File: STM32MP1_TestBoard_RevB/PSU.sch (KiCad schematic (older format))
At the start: 22 parts, among them J9 Barrel_Jack, Q1 DMG2302U, U3 SE8233X2, U4 TPS54202DDC

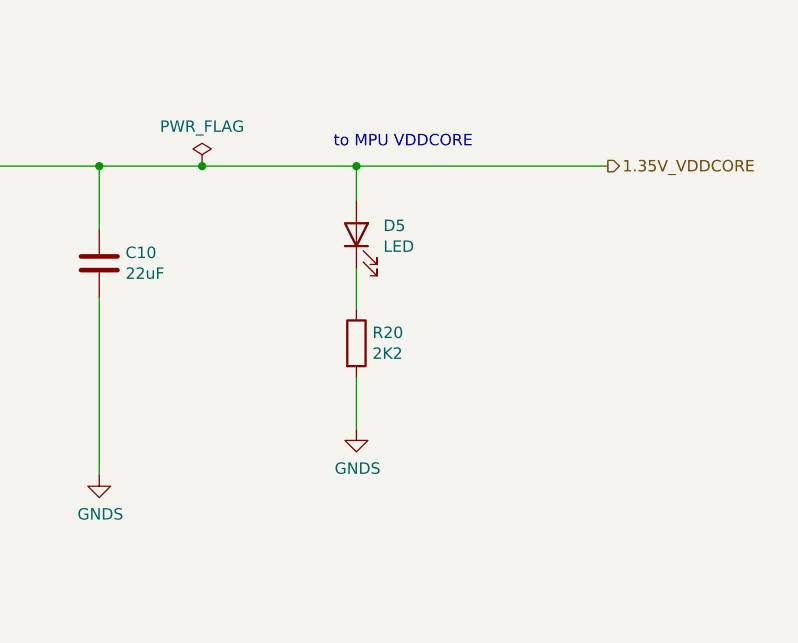
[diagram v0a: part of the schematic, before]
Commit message: Removed 1.35V led and unused DDR capacitors
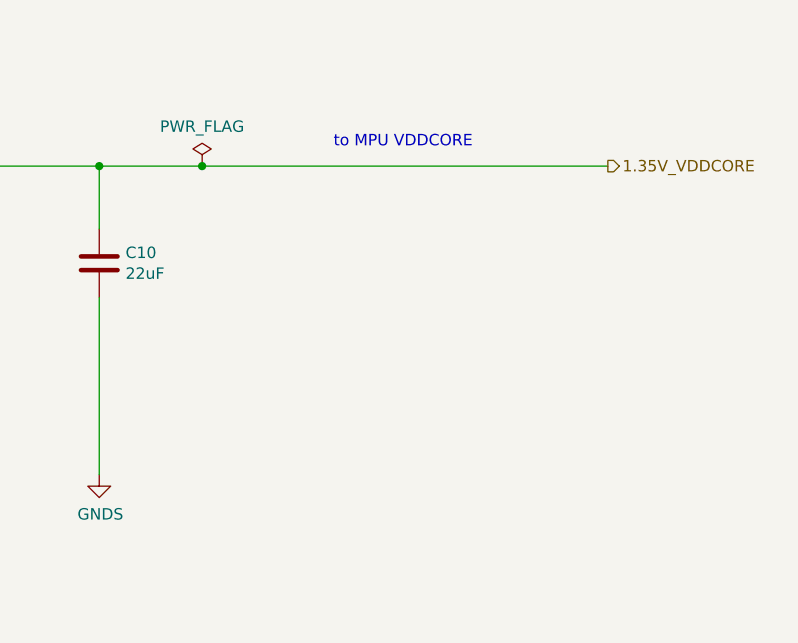
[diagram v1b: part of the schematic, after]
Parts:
- removed D5: LED, LED_SMD:LED_0805_2012Metric_Pad1.15x1.40mm_HandSolder, symbol Device:LED
- removed R20: 2K2, Resistor_SMD:R_0402_1005Metric_Pad0.72x0.64mm_HandSolder, symbol Device:R
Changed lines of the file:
@@
 Connection ~ 10950 4500
-Wire Wire Line
-	10950 4500 11625 4500
 Wire Wire Line
 	6250 8100 7575 8100
@@
 $EndComp
 $Comp
-L Device:LED D5
-U 1 1 5FCE57D0
-P 11625 4800
-F 0 "D5" V 11664 4682 50  0000 R CNN
-F 1 "LED" V 11573 4682 50  0000 R CNN
-F 2 "LED_SMD:LED_0805_2012Metric_Pad1.15x1.40mm_HandSolder" H 11625 4800 50  0001 C CNN
-F 3 "~" H 11625 4800 50  0001 C CNN
-F 4 "~" H 11625 4800 50  0001 C CNN "Mfr"
-F 5 "~" H 11625 4800 50  0001 C CNN "PartNo"
-	1    11625 4800
-	0    -1   -1   0
-$EndComp
-Wire Wire Line
-	11625 4650 11625 4500
-Wire Wire Line
-	11625 4950 11625 5125
-$Comp
-L Device:R R20
-U 1 1 5FCE57DA
-P 11625 5275
-F 0 "R20" H 11695 5321 50  0000 L CNN
-F 1 "2K2" H 11695 5230 50  0000 L CNN
-F 2 "Resistor_SMD:R_0402_1005Metric_Pad0.72x0.64mm_HandSolder" V 11555 5275 50  0001 C CNN
-F 3 "~" H 11625 5275 50  0001 C CNN
-F 4 "~" H 11625 5275 50  0001 C CNN "Mfr"
-F 5 "~" H 11625 5275 50  0001 C CNN "PartNo"
-	1    11625 5275
-	1    0    0    -1
-$EndComp
-Wire Wire Line
-	11625 5425 11625 5650
-$Comp
-L power:GNDS #PWR04
-U 1 1 5FCE57E1
-P 11625 5650
-F 0 "#PWR04" H 11625 5400 50  0001 C CNN
-F 1 "GNDS" H 11630 5477 50  0000 C CNN
-F 2 "" H 11625 5650 50  0001 C CNN
-F 3 "" H 11625 5650 50  0001 C CNN
-	1    11625 5650
-	1    0    0    -1
-$EndComp
-Connection ~ 11625 4500
-Wire Wire Line
-	11625 4500 12725 4500
-$Comp
 L Device:LED D3
 U 1 1 5FCE9C97
@@
 Connection ~ 6250 8100
 NoConn ~ 5750 4600
+Wire Wire Line
+	10950 4500 12725 4500
 $EndSCHEMATC

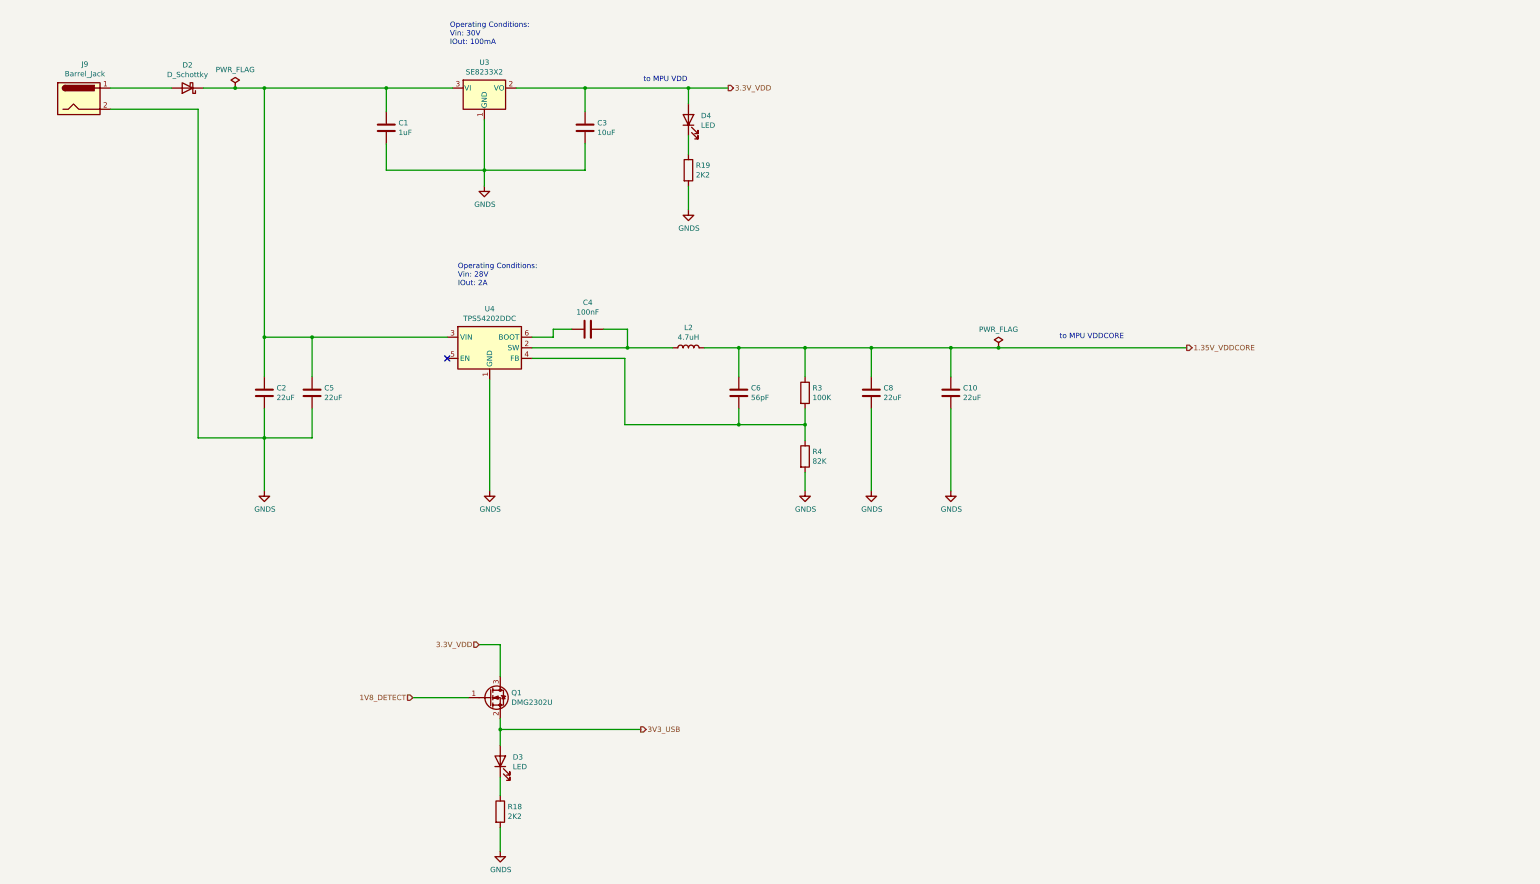
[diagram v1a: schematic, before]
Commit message: Updated design
- Added Crystal/Oscillators
- Replaced both SDMMC with single SDMMC w/ detect pin
- Added USB Type C for VIN
- Moved SWD pins
- Tidied up silk screen for pin headers J1, J2, J3, J4
- Moved DSI socket
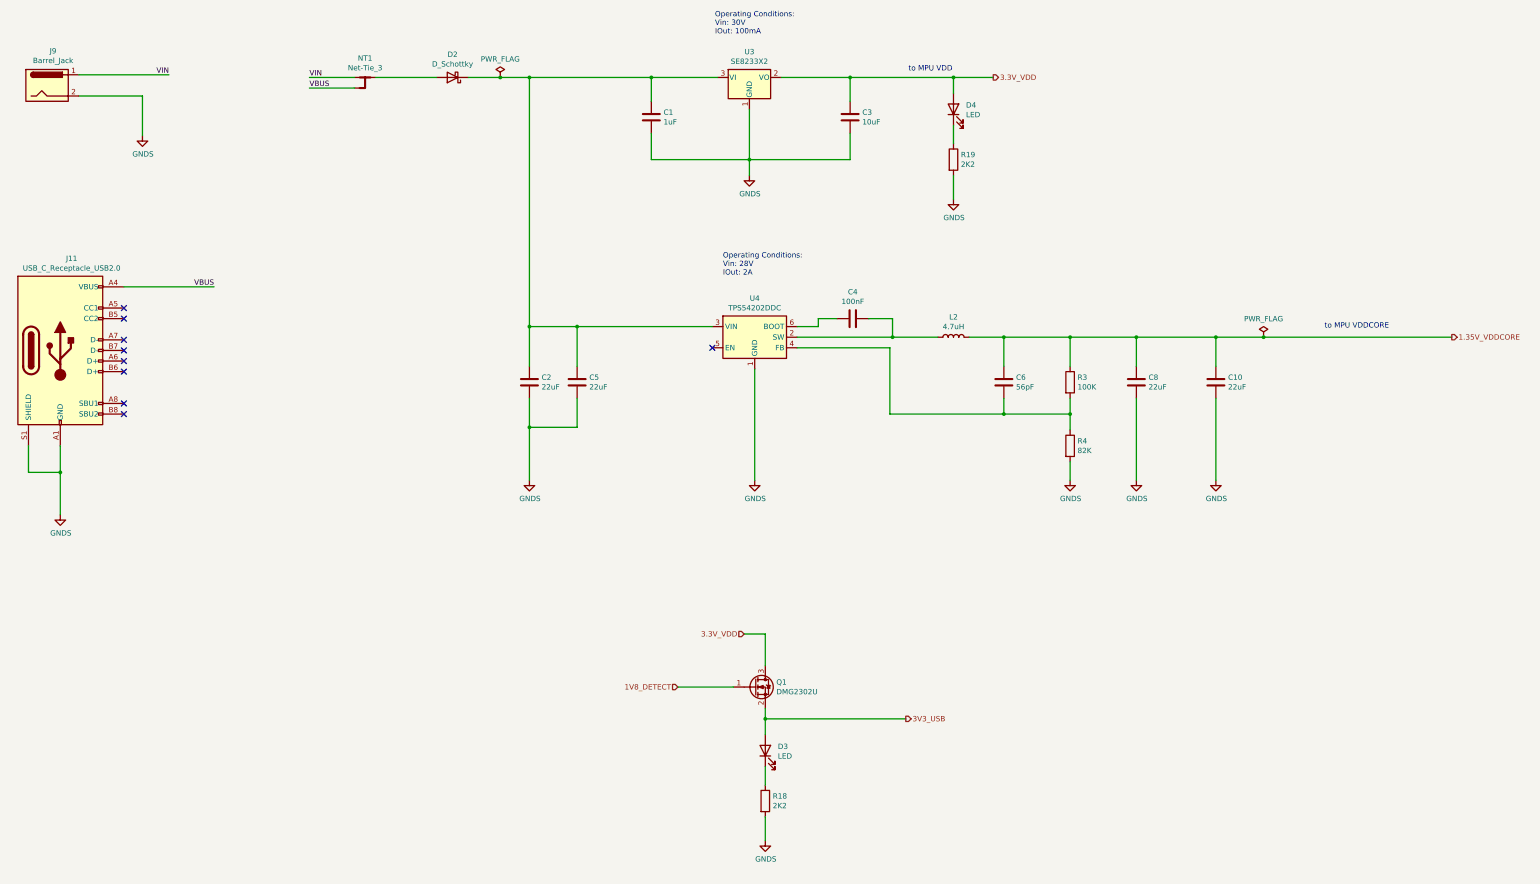
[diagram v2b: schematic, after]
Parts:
- added J11: USB_C_Receptacle_USB2.0, MolexUSB_TypeC:213716-0001_THT_Socket_RightAngle, symbol Connector:USB_C_Receptacle_USB2.0
- added NT1: Net-Tie_3, NetTie:NetTie-3_SMD_Pad0.5mm, symbol Device:Net-Tie_3
- C1: footprint Capacitor_SMD:C_0402_1005Metric_Pad0.74x0.62mm_HandSolder -> Capacitor_SMD:C_0805_2012Metric_Pad1.18x1.45mm_HandSolder; LCSC (none) -> C52923
- C3: footprint Capacitor_SMD:C_0402_1005Metric_Pad0.74x0.62mm_HandSolder -> Capacitor_SMD:C_0805_2012Metric_Pad1.18x1.45mm_HandSolder
- C4: LCSC (none) -> C49678
- C6: LCSC (none) -> C1828
- D3, D4: LCSC (none) -> C84256
- R3: LCSC (none) -> C17407
- R4: LCSC (none) -> C17840
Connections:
- net GNDS: now also J11.A1 (GND), J11.A12 (GND), J11.B1 (GND), J11.B12 (GND), J11.S1 (SHIELD)
- net at D2.2 (A): now also NT1.2; no longer J9.1
- new net VBUS: J11.A4 (VBUS), J11.A9 (VBUS), J11.B4 (VBUS), J11.B9 (VBUS), NT1.3
- new net VIN: J9.1, NT1.1
- no-connect marks 1 -> 9
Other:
- moved on the sheet: C1, C10, C2, C3, C4, C5, C6, C8, D2, D3, D4, J9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

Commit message: completed revb layout
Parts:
- removed D2: D_Schottky, Diode_SMD:D_SOD-123F, symbol Device:D_Schottky
- removed Q1: DMG2302U, Package_TO_SOT_SMD:SOT-23, symbol Device:Q_NMOS_GSD
- added C39, C43: 2.2uF, Capacitor_SMD:C_0805_2012Metric_Pad1.18x1.45mm_HandSolder, symbol Device:C
- added C41, C44: 100nF, Capacitor_SMD:C_0402_1005Metric_Pad0.74x0.62mm_HandSolder, symbol Device:C
- added D2: LED, LED_SMD:LED_0805_2012Metric_Pad1.15x1.40mm_HandSolder, symbol Device:LED
- added R26: 2K2, Resistor_SMD:R_0402_1005Metric_Pad0.72x0.64mm_HandSolder, symbol Device:R
- added U5, U6: SiP3250x, Package_TO_SOT_SMD:SOT-23-6_Handsoldering, symbol SiP3250x:SiP3250x
- C1: LCSC C52923 -> C28323
- J11: Mfr (none) -> Molex; Mouser (none) -> 538-213716-0001; PartNo (none) -> 213716-0001
- R18, R19: LCSC (none) -> C25879
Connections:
- net 1.35V_VDDCORE: now also U6.3 (EN)
- net 1V8_DETECT: now also U5.3 (EN)
- net 3.3V_VDD: now also C39.1, C43.1, U5.5 (IN), U5.6 (IN), U6.5 (IN), U6.6 (IN)
- net 3V3_USB: now also C41.1, U5.1 (OUT), U5.2 (OUT)
- net GNDS: now also C39.2, C41.2, C43.2, C44.2, R26.2, U5.4 (GND), U6.4 (GND)
- net at C1.1, C2.1, C5.1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: now also NT1.2
- new net: C44.1, D2.2 (A), U6.1 (OUT), U6.2 (OUT)
- new net: D2.1 (K), R26.1
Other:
- note added: "1A Required"
- note added: "6.6mA Required Max"
- note removed: "to MPU VDD"
- note removed: "to MPU VDDCORE"
- moved on the sheet: D3, R18

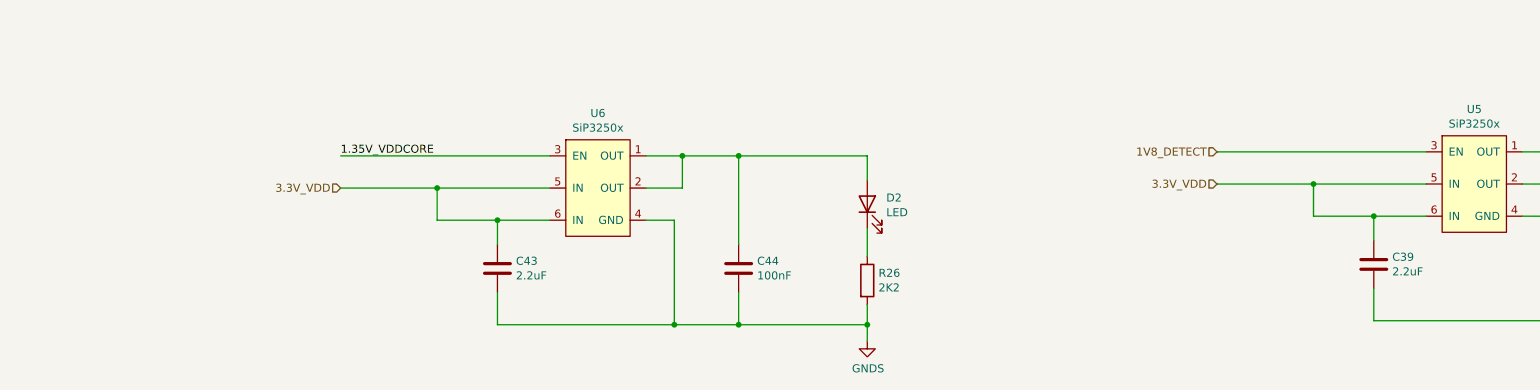
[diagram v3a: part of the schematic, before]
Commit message: updated revb
- Fixed MIPI DSI differential trace spacings. 
- Moved passive components onto back of pcb
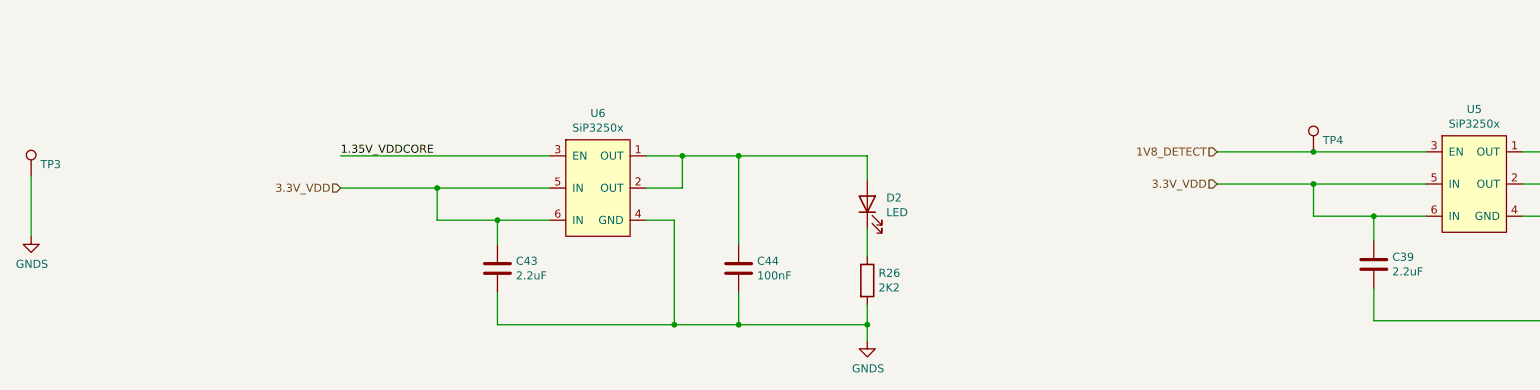
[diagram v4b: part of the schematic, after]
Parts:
- added TP3, TP4: TestPoint, TestPoint:TestPoint_Pad_D1.0mm, symbol Connector:TestPoint
- C1: footprint Capacitor_SMD:C_0805_2012Metric_Pad1.18x1.45mm_HandSolder -> Capacitor_SMD:C_0402_1005Metric_Pad0.74x0.62mm_HandSolder; LCSC C28323 -> C52923
- C3: footprint Capacitor_SMD:C_0805_2012Metric_Pad1.18x1.45mm_HandSolder -> Capacitor_SMD:C_0402_1005Metric_Pad0.74x0.62mm_HandSolder; LCSC (none) -> C15525
- C39, C43: footprint Capacitor_SMD:C_0805_2012Metric_Pad1.18x1.45mm_HandSolder -> Capacitor_SMD:C_0603_1608Metric_Pad1.08x0.95mm_HandSolder; LCSC C49217 -> C23630
- C4: footprint Capacitor_SMD:C_0805_2012Metric_Pad1.18x1.45mm_HandSolder -> Capacitor_SMD:C_0402_1005Metric_Pad0.74x0.62mm_HandSolder; LCSC C49678 -> C1525
- C6: footprint Capacitor_SMD:C_0805_2012Metric_Pad1.18x1.45mm_HandSolder -> Capacitor_SMD:C_0402_1005Metric_Pad0.74x0.62mm_HandSolder; LCSC C1828 -> C1572
- R3: footprint Resistor_SMD:R_0805_2012Metric_Pad1.20x1.40mm_HandSolder -> Resistor_SMD:R_0402_1005Metric_Pad0.72x0.64mm_HandSolder; LCSC C17407 -> C25741
- R4: footprint Resistor_SMD:R_0805_2012Metric_Pad1.20x1.40mm_HandSolder -> Resistor_SMD:R_0402_1005Metric_Pad0.72x0.64mm_HandSolder; LCSC C17840 -> C1542
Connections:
- net 1V8_DETECT: now also TP4.1
- net GNDS: now also TP3.1
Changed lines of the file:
@@
 F 0 "C4" V 9323 4225 50  0000 C CNN
 F 1 "100nF" V 9414 4225 50  0000 C CNN
-F 2 "Capacitor_SMD:C_0805_2012Metric_Pad1.18x1.45mm_HandSolder" H 9613 4075 50  0001 C CNN
+F 2 "Capacitor_SMD:C_0402_1005Metric_Pad0.74x0.62mm_HandSolder" H 9613 4075 50  0001 C CNN
 F 3 "~" H 9575 4225 50  0001 C CNN
 F 4 "~" H 9575 4225 50  0001 C CNN "Mfr"
 F 5 "~" H 9575 4225 50  0001 C CNN "PartNo"
-F 6 "C49678" H 9575 4225 50  0001 C CNN "LCSC"
+F 6 "C1525" H 9575 4225 50  0001 C CNN "LCSC"
 F 7 "~" H 9575 4225 50  0001 C CNN "Comment"
 F 8 "~" H 9575 4225 50  0001 C CNN "Mouser"
@@
 F 0 "C6" H 10885 4779 50  0000 R CNN
 F 1 "56pF" H 10885 4870 50  0000 R CNN
-F 2 "Capacitor_SMD:C_0805_2012Metric_Pad1.18x1.45mm_HandSolder" H 11038 4675 50  0001 C CNN
+F 2 "Capacitor_SMD:C_0402_1005Metric_Pad0.74x0.62mm_HandSolder" H 11038 4675 50  0001 C CNN
 F 3 "~" H 11000 4825 50  0001 C CNN
 F 4 "~" H 11000 4825 50  0001 C CNN "Mfr"
 F 5 "~" H 11000 4825 50  0001 C CNN "PartNo"
-F 6 "C1828" H 11000 4825 50  0001 C CNN "LCSC"
+F 6 "C1572" H 11000 4825 50  0001 C CNN "LCSC"
 F 7 "~" H 11000 4825 50  0001 C CNN "Comment"
 F 8 "~" H 11000 4825 50  0001 C CNN "Mouser"
@@
 F 0 "R3" H 11695 4871 50  0000 L CNN
 F 1 "100K" H 11695 4780 50  0000 L CNN
-F 2 "Resistor_SMD:R_0805_2012Metric_Pad1.20x1.40mm_HandSolder" V 11555 4825 50  0001 C CNN
+F 2 "Resistor_SMD:R_0402_1005Metric_Pad0.72x0.64mm_HandSolder" V 11555 4825 50  0001 C CNN
 F 3 "~" H 11625 4825 50  0001 C CNN
 F 4 "~" H 11625 4825 50  0001 C CNN "Mfr"
 F 5 "~" H 11625 4825 50  0001 C CNN "PartNo"
-F 6 "C17407" H 11625 4825 50  0001 C CNN "LCSC"
+F 6 "C25741" H 11625 4825 50  0001 C CNN "LCSC"
 F 7 "~" H 11625 4825 50  0001 C CNN "Comment"
 F 8 "~" H 11625 4825 50  0001 C CNN "Mouser"
@@
 F 0 "R4" H 11695 5471 50  0000 L CNN
 F 1 "82K" H 11695 5380 50  0000 L CNN
-F 2 "Resistor_SMD:R_0805_2012Metric_Pad1.20x1.40mm_HandSolder" V 11555 5425 50  0001 C CNN
+F 2 "Resistor_SMD:R_0402_1005Metric_Pad0.72x0.64mm_HandSolder" V 11555 5425 50  0001 C CNN
 F 3 "~" H 11625 5425 50  0001 C CNN
 F 4 "~" H 11625 5425 50  0001 C CNN "Mfr"
 F 5 "~" H 11625 5425 50  0001 C CNN "PartNo"
-F 6 "C17840" H 11625 5425 50  0001 C CNN "LCSC"
+F 6 "C1542" H 11625 5425 50  0001 C CNN "LCSC"
 F 7 "~" H 11625 5425 50  0001 C CNN "Comment"
 F 8 "~" H 11625 5425 50  0001 C CNN "Mouser"
@@
 Text HLabel 12900 7675 2    50   Output ~ 0
 3V3_USB
-Wire Wire Line
-	10400 7675 9100 7675
 $Comp
 L power:PWR_FLAG #FLG0102
@@
 F 0 "C1" H 7790 2371 50  0000 L CNN
 F 1 "1uF" H 7790 2280 50  0000 L CNN
-F 2 "Capacitor_SMD:C_0805_2012Metric_Pad1.18x1.45mm_HandSolder" H 7713 2175 50  0001 C CNN
+F 2 "Capacitor_SMD:C_0402_1005Metric_Pad0.74x0.62mm_HandSolder" H 7713 2175 50  0001 C CNN
 F 3 "~" H 7675 2325 50  0001 C CNN
 F 4 "~" H 7675 2325 50  0001 C CNN "Mfr"
 F 5 "~" H 7675 2325 50  0001 C CNN "PartNo"
-F 6 "C28323" H 7675 2325 50  0001 C CNN "LCSC"
+F 6 "C52923" H 7675 2325 50  0001 C CNN "LCSC"
 F 7 "~" H 7675 2325 50  0001 C CNN "Comment"
 F 8 "~" H 7675 2325 50  0001 C CNN "Mouser"
@@
 F 0 "C3" H 9435 2371 50  0000 R CNN
 F 1 "10uF" H 9435 2280 50  0000 R CNN
-F 2 "Capacitor_SMD:C_0805_2012Metric_Pad1.18x1.45mm_HandSolder" H 9588 2175 50  0001 C CNN
+F 2 "Capacitor_SMD:C_0402_1005Metric_Pad0.74x0.62mm_HandSolder" H 9588 2175 50  0001 C CNN
 F 3 "~" H 9550 2325 50  0001 C CNN
 F 4 "~" H 9550 2325 50  0001 C CNN "Mfr"
 F 5 "~" H 9550 2325 50  0001 C CNN "PartNo"
-F 6 "~" H 9550 2325 50  0001 C CNN "LCSC"
+F 6 "C15525" H 9550 2325 50  0001 C CNN "LCSC"
 F 7 "~" H 9550 2325 50  0001 C CNN "Comment"
 F 8 "~" H 9550 2325 50  0001 C CNN "Mouser"
@@
 F 0 "C39" H 10190 8421 50  0000 L CNN
 F 1 "2.2uF" H 10190 8330 50  0000 L CNN
-F 2 "Capacitor_SMD:C_0805_2012Metric_Pad1.18x1.45mm_HandSolder" H 10113 8225 50  0001 C CNN
+F 2 "Capacitor_SMD:C_0603_1608Metric_Pad1.08x0.95mm_HandSolder" H 10113 8225 50  0001 C CNN
 F 3 "~" H 10075 8375 50  0001 C CNN
-F 4 "C49217" H 10075 8375 50  0001 C CNN "LCSC"
+F 4 "C23630" H 10075 8375 50  0001 C CNN "LCSC"
 F 5 "~" H 10075 8375 50  0001 C CNN "Mfr"
 F 6 "~" H 10075 8375 50  0001 C CNN "Mouser"
@@
 Wire Wire Line
 	11575 7675 12375 7675
-Wire Wire Line
-	4950 7700 3650 7700
 Text HLabel 3650 7900 0    50   Input ~ 0
 3.3V_VDD
@@
 Connection ~ 5725 8750
 $Comp
-L Device:C C43
-U 1 1 6070B3C2
-P 4625 8400
-F 0 "C43" H 4740 8446 50  0000 L CNN
-F 1 "2.2uF" H 4740 8355 50  0000 L CNN
-F 2 "Capacitor_SMD:C_0805_2012Metric_Pad1.18x1.45mm_HandSolder" H 4663 8250 50  0001 C CNN
-F 3 "~" H 4625 8400 50  0001 C CNN
-F 4 "C49217" H 4625 8400 50  0001 C CNN "LCSC"
-F 5 "~" H 4625 8400 50  0001 C CNN "Mfr"
-F 6 "~" H 4625 8400 50  0001 C CNN "Mouser"
-F 7 "~" H 4625 8400 50  0001 C CNN "PartNo"
-	1    4625 8400
-	1    0    0    -1
-$EndComp
-$Comp
 L Device:C C44
 U 1 1 6070B3C8
@@
 Wire Wire Line
 	2700 3925 3550 3925
+$Comp
+L Device:C C43
+U 1 1 6070B3C2
+P 4625 8400
+F 0 "C43" H 4740 8446 50  0000 L CNN
+F 1 "2.2uF" H 4740 8355 50  0000 L CNN
+F 2 "Capacitor_SMD:C_0603_1608Metric_Pad1.08x0.95mm_HandSolder" H 4663 8250 50  0001 C CNN
+F 3 "~" H 4625 8400 50  0001 C CNN
+F 4 "C23630" H 4625 8400 50  0001 C CNN "LCSC"
+F 5 "~" H 4625 8400 50  0001 C CNN "Mfr"
+F 6 "~" H 4625 8400 50  0001 C CNN "Mouser"
+F 7 "~" H 4625 8400 50  0001 C CNN "PartNo"
+	1    4625 8400
+	1    0    0    -1
+$EndComp
+Wire Wire Line
+	10400 7675 9700 7675
+Wire Wire Line
+	4950 7700 3650 7700
+$Comp
+L Connector:TestPoint TP4
+U 1 1 607E46DE
+P 9700 7675
+F 0 "TP4" H 9758 7747 50  0000 L CNN
+F 1 "TestPoint" H 9758 7702 50  0001 L CNN
+F 2 "TestPoint:TestPoint_Pad_D1.0mm" H 9900 7675 50  0001 C CNN
+F 3 "~" H 9900 7675 50  0001 C CNN
+	1    9700 7675
+	1    0    0    -1
+$EndComp
+Connection ~ 9700 7675
+Wire Wire Line
+	9700 7675 9100 7675
+$Comp
+L Connector:TestPoint TP3
+U 1 1 607F3316
+P 1725 7825
+F 0 "TP3" H 1783 7897 50  0000 L CNN
+F 1 "TestPoint" H 1783 7852 50  0001 L CNN
+F 2 "TestPoint:TestPoint_Pad_D1.0mm" H 1925 7825 50  0001 C CNN
+F 3 "~" H 1925 7825 50  0001 C CNN
+	1    1725 7825
+	1    0    0    -1
+$EndComp
+Wire Wire Line
+	1725 7825 1725 8200
+$Comp
+L power:GNDS #PWR0114
+U 1 1 607FB93E
+P 1725 8200
+F 0 "#PWR0114" H 1725 7950 50  0001 C CNN
+F 1 "GNDS" H 1730 8027 50  0000 C CNN
+F 2 "" H 1725 8200 50  0001 C CNN
+F 3 "" H 1725 8200 50  0001 C CNN
+	1    1725 8200
+	1    0    0    -1
+$EndComp
 $EndSCHEMATC
